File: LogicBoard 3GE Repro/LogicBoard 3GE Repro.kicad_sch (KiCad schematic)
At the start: 161 parts, among them IC201 27C512PLCC, IC204 CY62256-70PC, IC206 MC6809E, IC207 6522, IC208 YM2149, IC209 74HC74, IC301 MC1408, IC302 CD4052B, IC303 LF347, IC304 LF353, IC305 4066, J201 CART, J202 DB9_Male, J203 DB9_Male, J204 Power, J301 Video, J302 Audio, Q301 2N3905, Q302 2N3905, Q303 2N3904, SW201 Reset, U1 ATF16V8Bxx-xxPU

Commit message: Repro: on-board LM386 audio amp (anti-buzz) + external volume
Added IC306 LM386 audio amp on the logic board (next to YM2149, GNDA ref)
to avoid the cross-board low-level audio run that causes Vectrex buzz.
AUDIO -> J304 (panel volume pot) -> LM386 -> J303 speaker. Removed J302
line-out. ERC 11.

Co-Authored-By: Claude Opus 4.8 <noreply@anthropic.com>
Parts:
- removed C227: 22uF, Capacitor_SMD:C_1206_3216Metric, symbol Device:C_Polarized_Small
- removed C228: 22uF 16V, Capacitor_SMD:C_1206_3216Metric, symbol Device:C_Polarized_Small
- removed C323: 4.7uF 16V, Capacitor_SMD:C_0805_2012Metric, symbol Device:C_Polarized_Small
- removed J302: Audio, Connector_Molex:Molex_KK-254_AE-6410-02A_1x02_P2.54mm_Vertical, symbol Connector_Generic:Conn_01x02
- added C227, C228: 22uF, Capacitor_SMD:C_1206_3216Metric, symbol Device:C_Small
- added C323: 4.7uF 16V, Capacitor_SMD:C_0805_2012Metric, symbol Device:C_Small
- added C329, C331: 0.1uF, Capacitor_SMD:C_0402_1005Metric, symbol Device:C_Small
- added C330: 10uF, Capacitor_SMD:C_0402_1005Metric, symbol Device:C_Small
- added C332: C_Polarized_Small, symbol Device:C_Polarized_Small
- added C333: 47nF, Capacitor_SMD:C_0402_1005Metric, symbol Device:C_Small
- added IC306: LM386, symbol Amplifier_Audio:LM386
- added J303: Speaker, symbol Connector_Generic:Conn_01x02
- added J304: Volume, symbol Connector_Generic:Conn_01x03
- added R347: 10, symbol Device:R_Small
- added R348: 10K, symbol Device:R_Small
- D201, D301, D302: footprint (none) -> Diode_SMD:D_SOD-123
- IC201: footprint (none) -> Package_LCC:PLCC-32_THT-Socket
- IC202: renamed from U1; footprint (none) -> Package_SO:SOIC-20W_7.5x12.8mm_P1.27mm
- IC204: footprint (none) -> Package_SO:SOP-28_8.4x18.16mm_P1.27mm
- IC206, IC207: footprint (none) -> Package_LCC:PLCC-44_SMD-Socket
- IC208: footprint (none) -> Package_DIP:DIP-40_W15.24mm_Socket
- IC209, IC303, IC305: footprint (none) -> Package_SO:SOIC-14_3.9x8.7mm_P1.27mm
- IC301, IC302: footprint (none) -> Package_SO:SOIC-16_3.9x9.9mm_P1.27mm
- IC304: footprint (none) -> Package_SO:SOIC-8_3.9x4.9mm_P1.27mm
- J201: footprint (none) -> Vectrex LogicBoard:SULLINS_EBC18DRAS
- JP1, JP2, JP3: footprint (none) -> Connector_PinHeader_2.54mm:PinHeader_1x03_P2.54mm_Vertical
- Q301, Q302, Q303: footprint (none) -> Package_TO_SOT_SMD:SOT-23
- SW201: footprint (none) -> Connector_PinHeader_2.54mm:PinHeader_1x02_P2.54mm_Horizontal
- W1, W2, W3: footprint (none) -> NetTie:NetTie-2_SMD_Pad0.5mm
- Y201: renamed from OSC1; footprint (none) -> Oscillator:Oscillator_SMD_EuroQuartz_XO32-4Pin_3.2x2.5mm
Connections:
- net +5V: now also C227.1, C331.2, IC306.6 (V+)
- net AUDIO: now also J304.1 (Pin_1)
- net CH(A+B+C): now also C323.1
- net CH(A+B+C)+DIGITAL_AUDIO: now also C323.2
- net GNDA: now also C330.1, C331.1, C333.2, IC306.2 (-), IC306.4 (GND), J303.2 (Pin_2), J304.3 (Pin_3), R348.1
- net GNDD: now also C227.2, C228.2
- net ~{RESET}: now also C228.1
- new net: C330.2, IC306.7 (BYPASS)
- new net: C332.2, J303.1 (Pin_1)
- new net: C329.1, IC306.3 (+), R348.2
- new net: C329.2, J304.2 (Pin_2)
- new net: C332.1, IC306.5, R347.2
- new net: C333.1, R347.1
- no-connect marks 17 -> 18

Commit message: Repro: Phase 2 complete - all footprints assigned + audio amp
170 components, all footprints assigned (SMD 0402/SOIC/SOP/PLCC sockets,
3296W trimmers, LM386 audio amp). Integrator caps C0G, electrolytics
polarized, no polarity mismatches. Schematic + footprints done, ERC 11
(all intentional/trivial). Ready for PCB layout.

Co-Authored-By: Claude Opus 4.8 <noreply@anthropic.com>
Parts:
- C332, R348: footprint (none) -> Capacitor_SMD:CP_Elec_8x10.5
- IC306: footprint (none) -> Package_SO:SOIC-8_3.9x4.9mm_P1.27mm
- J303: footprint (none) -> Connector_PinHeader_2.54mm:PinHeader_1x02_P2.54mm_Vertical
- J304: footprint (none) -> Connector_PinHeader_2.54mm:PinHeader_1x03_P2.54mm_Vertical
- R302, R326, R333, R335: footprint Resistor_SMD:R_0402_1005Metric -> Potentiometer_THT:Potentiometer_Bourns_3296W_Vertical
- R347: footprint (none) -> Resistor_SMD:R_0402_1005Metric
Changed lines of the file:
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@@
 			)
 		)
-		(property "Footprint" "Resistor_SMD:R_0402_1005Metric"
+		(property "Footprint" "Potentiometer_THT:Potentiometer_Bourns_3296W_Vertical"
 			(at 146.05 147.32 0)
 			(hide yes)
@@
 			)
 		)
-		(property "Footprint" ""
+		(property "Footprint" "Connector_PinHeader_2.54mm:PinHeader_1x02_P2.54mm_Vertical"
 			(at 497.84 68.58 0)
 			(hide yes)
@@
 			)
 		)
-		(property "Footprint" ""
+		(property "Footprint" "Capacitor_SMD:CP_Elec_8x10.5"
 			(at 476.25 26.67 0)
 			(hide yes)
@@
 			)
 		)
-		(property "Footprint" ""
+		(property "Footprint" "Package_SO:SOIC-8_3.9x4.9mm_P1.27mm"
 			(at 491.49 39.37 0)
 			(hide yes)
@@
 			)
 		)
-		(property "Footprint" "Resistor_SMD:R_0402_1005Metric"
+		(property "Footprint" "Potentiometer_THT:Potentiometer_Bourns_3296W_Vertical"
 			(at 181.61 134.62 0)
 			(hide yes)
@@
 			)
 		)
-		(property "Footprint" "Resistor_SMD:R_0402_1005Metric"
+		(property "Footprint" "Potentiometer_THT:Potentiometer_Bourns_3296W_Vertical"
 			(at 181.61 255.27 0)
 			(hide yes)
@@
 			)
 		)
-		(property "Footprint" ""
+		(property "Footprint" "Resistor_SMD:R_0402_1005Metric"
 			(at 486.41 50.8 0)
 			(hide yes)
@@
 			)
 		)
-		(property "Footprint" ""
+		(property "Footprint" "Capacitor_SMD:CP_Elec_8x10.5"
 			(at 490.22 62.23 0)
 			(hide yes)
@@
 			)
 		)
-		(property "Footprint" ""
+		(property "Footprint" "Connector_PinHeader_2.54mm:PinHeader_1x03_P2.54mm_Vertical"
 			(at 491.49 7.62 0)
 			(hide yes)
@@
 			)
 		)
-		(property "Footprint" "Resistor_SMD:R_0402_1005Metric"
+		(property "Footprint" "Potentiometer_THT:Potentiometer_Bourns_3296W_Vertical"
 			(at 76.2 146.05 0)
 			(hide yes)

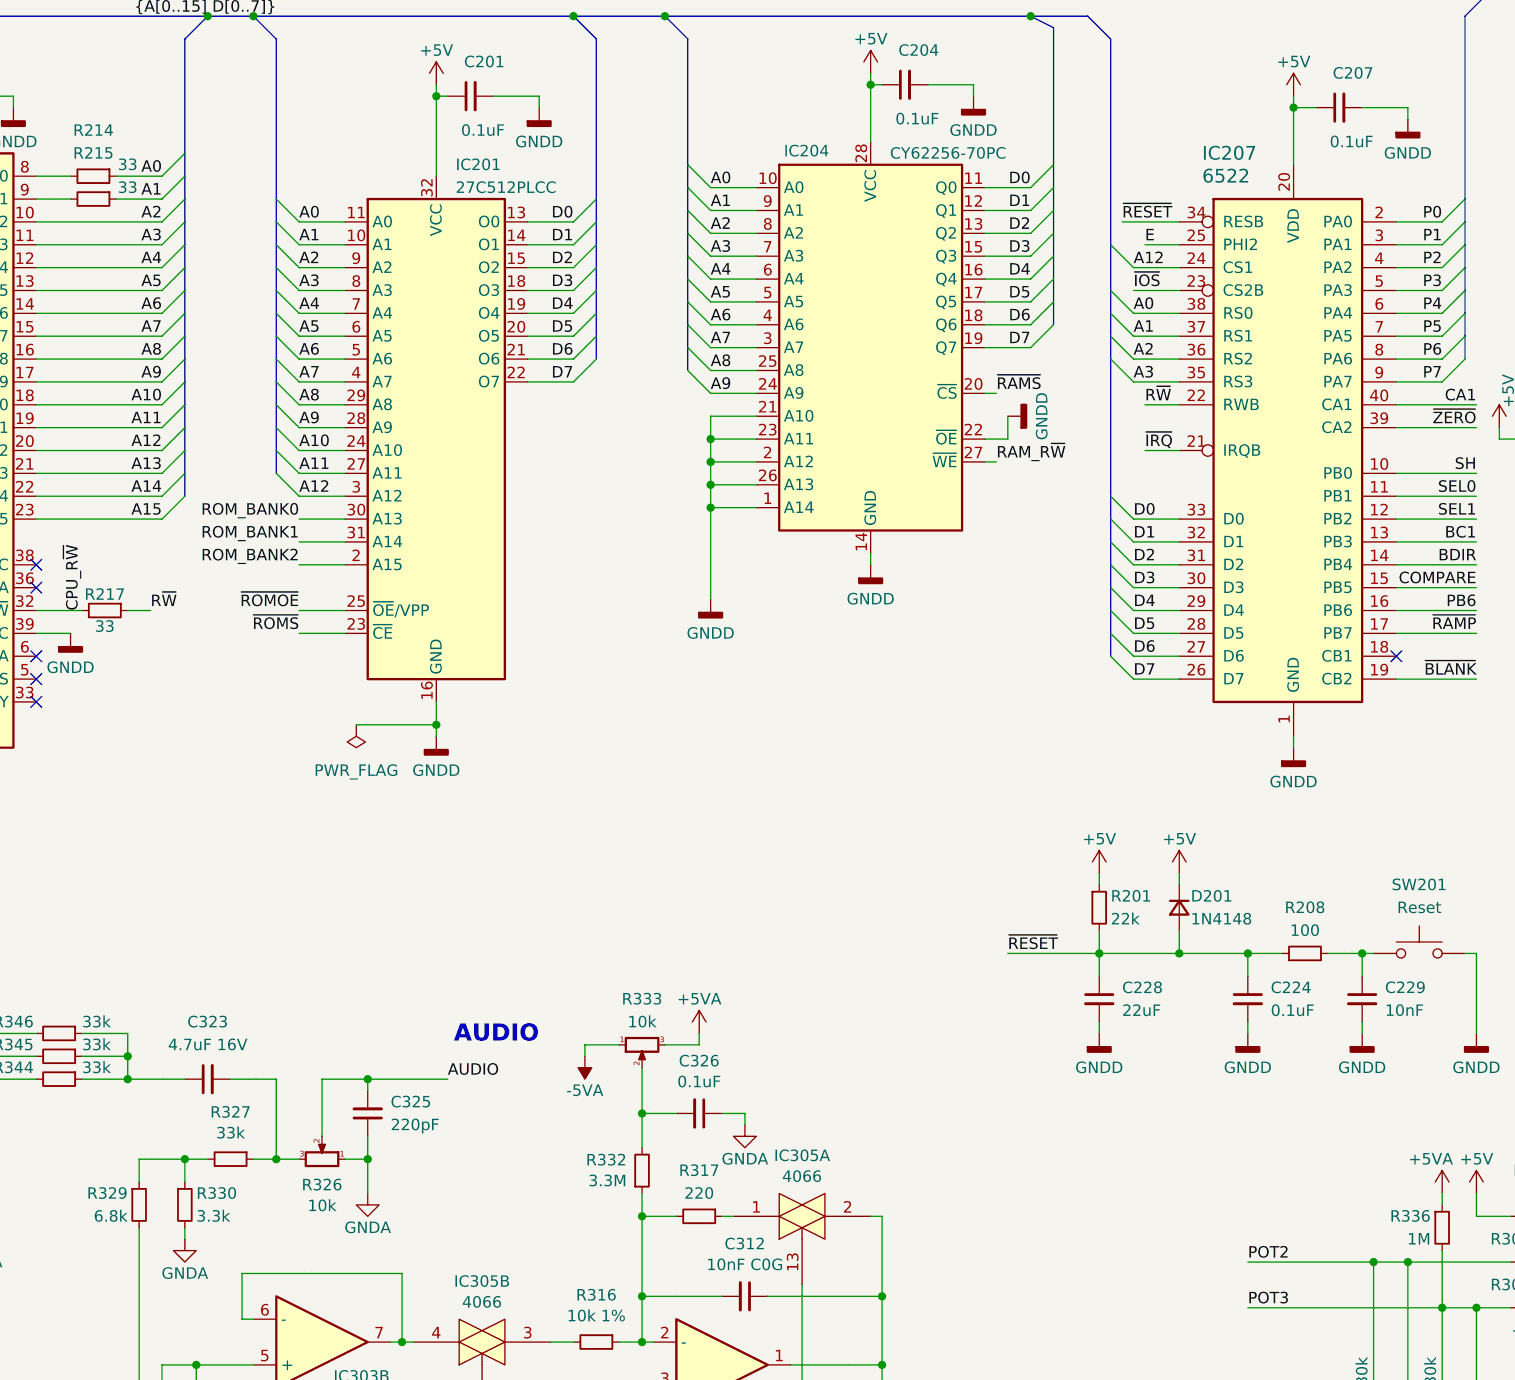
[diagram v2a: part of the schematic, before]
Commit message: Repro: remove redundant R326 volume pot (volume now single, in preamp)
R326 was the original Vectrex preamp volume pot; redundant now that the
external panel pot (J304) does it. Removed R326, merged the channel-mix
node into AUDIO -> J304 -> LM386. 3 calibration trimmers remain
(R302/R333/R335). ERC 11.

Co-Authored-By: Claude Opus 4.8 <noreply@anthropic.com>
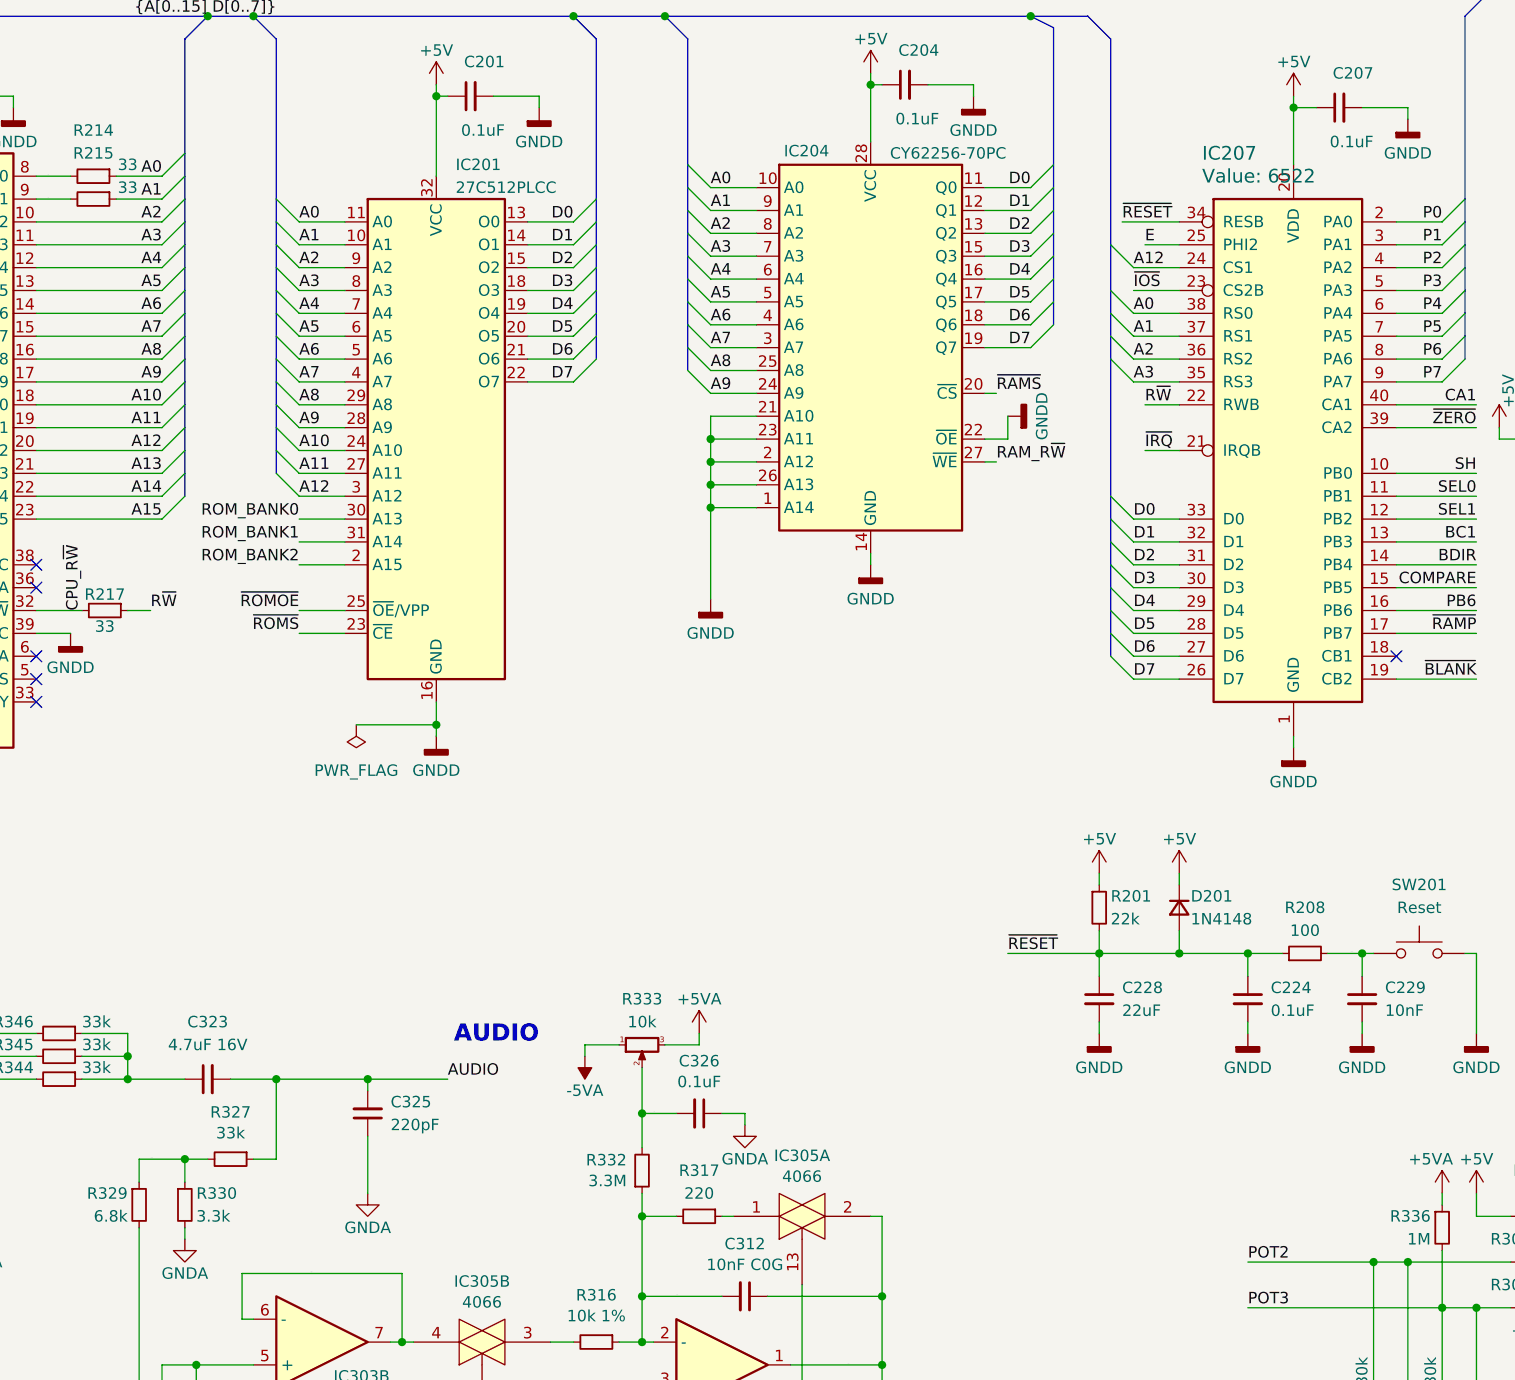
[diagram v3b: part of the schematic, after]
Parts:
- removed R326: 10k, Potentiometer_THT:Potentiometer_Bourns_3296W_Vertical, symbol Device:R_Potentiometer_Small
- R348: footprint Capacitor_SMD:CP_Elec_8x10.5 -> Resistor_SMD:R_0402_1005Metric
- SW201: footprint Connector_PinHeader_2.54mm:PinHeader_1x02_P2.54mm_Horizontal -> Connector_PinHeader_2.54mm:PinHeader_1x02_P2.54mm_Vertical
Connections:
- net CH(A+B+C)+DIGITAL_AUDIO is gone; now on net AUDIO: C323.2, R327.1
- net CH(A+B+C): no longer names the net of C323.1, R344.1, R345.1, R346.1
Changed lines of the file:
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@@
 	)
 	(junction
-		(at 151.13 147.32)
-		(diameter 0)
-		(color 0 0 0 0)
-	)
-	(junction
 		(at 36.83 196.85)
 		(diameter 0)
@@
 	)
 	(junction
-		(at 140.97 147.32)
-		(diameter 0)
-		(color 0 0 0 0)
-	)
-	(junction
 		(at 323.85 148.59)
 		(diameter 0)
@@
 	)
 	(junction
+		(at 140.97 138.43)
+		(diameter 0)
+		(color 0 0 0 0)
+	)
+	(junction
 		(at 328.93 223.52)
 		(diameter 0)
@@
 	(wire
 		(pts
+			(xy 140.97 138.43) (xy 140.97 147.32)
+		)
+		(stroke
+			(width 0)
+			(type default)
+		)
+	)
+	(wire
+		(pts
 			(xy 355.6 153.67) (xy 355.6 184.15)
 		)
@@
 	(wire
 		(pts
-			(xy 140.97 147.32) (xy 143.51 147.32)
-		)
-		(stroke
-			(width 0)
-			(type default)
-		)
-	)
-	(wire
-		(pts
 			(xy 45.72 55.88) (xy 55.88 55.88)
 		)
@@
 	(wire
 		(pts
-			(xy 151.13 147.32) (xy 151.13 151.13)
+			(xy 151.13 144.78) (xy 151.13 151.13)
 		)
 		(stroke
@@
 	(wire
 		(pts
-			(xy 151.13 144.78) (xy 151.13 147.32)
-		)
-		(stroke
-			(width 0)
-			(type default)
-		)
-	)
-	(wire
-		(pts
 			(xy 347.98 172.72) (xy 367.03 172.72)
 		)
@@
 	(wire
 		(pts
-			(xy 140.97 147.32) (xy 140.97 138.43)
-		)
-		(stroke
-			(width 0)
-			(type default)
-		)
-	)
-	(wire
-		(pts
 			(xy 270.51 151.13) (xy 270.51 152.4)
 		)
@@
 	(wire
 		(pts
-			(xy 148.59 147.32) (xy 151.13 147.32)
-		)
-		(stroke
-			(width 0)
-			(type default)
-		)
-	)
-	(wire
-		(pts
 			(xy 189.23 46.99) (xy 194.31 46.99)
 		)
@@
 	(wire
 		(pts
-			(xy 146.05 138.43) (xy 151.13 138.43)
-		)
-		(stroke
-			(width 0)
-			(type default)
-		)
-	)
-	(wire
-		(pts
 			(xy 114.3 63.5) (xy 128.27 63.5)
 		)
@@
 	(wire
 		(pts
+			(xy 135.89 138.43) (xy 151.13 138.43)
+		)
+		(stroke
+			(width 0)
+			(type default)
+		)
+	)
+	(wire
+		(pts
 			(xy 45.72 66.04) (xy 55.88 66.04)
 		)
@@
 	(wire
 		(pts
-			(xy 146.05 138.43) (xy 146.05 144.78)
-		)
-		(stroke
-			(width 0)
-			(type default)
-		)
-	)
-	(wire
-		(pts
 			(xy 317.5 218.44) (xy 317.5 223.52)
 		)
@@
 	(wire
 		(pts
-			(xy 140.97 138.43) (xy 135.89 138.43)
-		)
-		(stroke
-			(width 0)
-			(type default)
-		)
-	)
-	(wire
-		(pts
 			(xy 143.51 88.9) (xy 148.59 88.9)
 		)
@@
 		)
 	)
-	(label "CH(A+B+C)+DIGITAL_AUDIO"
-		(at 138.43 138.43 0)
-		(effects
-			(font
-				(size 0.0254 0.0254)
-			)
-			(justify left bottom)
-		)
-	)
 	(label "RAM_R~{W}"
 		(at 220.98 69.85 0)
@@
 		)
 	)
-	(label "CH(A+B+C)"
-		(at 128.27 138.43 0)
-		(effects
-			(font
-				(size 0.0254 0.0254)
-			)
-			(justify left bottom)
-		)
-	)
 	(label "A2"
 		(at 189.23 44.45 0)
@@
 	)
 	(symbol
-		(lib_id "Device:R_Potentiometer_Small")
-		(at 146.05 147.32 270)
-		(mirror x)
-		(unit 1)
-		(body_style 1)
-		(exclude_from_sim no)
-		(in_bom yes)
-		(on_board yes)
-		(in_pos_files yes)
-		(dnp no)
-		(property "Reference" "R326"
-			(at 146.05 150.1902 90)
-			(show_name no)
-			(do_not_autoplace no)
-			(effects
-				(font
-					(size 1.27 1.27)
-				)
-			)
-		)
-		(property "Value" "10k"
-			(at 146.05 152.5016 90)
-			(show_name no)
-			(do_not_autoplace no)
-			(effects
-				(font
-					(size 1.27 1.27)
-				)
-			)
-		)
-		(property "Footprint" "Potentiometer_THT:Potentiometer_Bourns_3296W_Vertical"
-			(at 146.05 147.32 0)
-			(hide yes)
-			(show_name no)
-			(do_not_autoplace no)
-			(effects
-				(font
-					(size 1.27 1.27)
-				)
-			)
-		)
-		(property "Datasheet" ""
-			(at 146.05 147.32 0)
-			(hide yes)
-			(show_name no)
-			(do_not_autoplace no)
-			(effects
-				(font
-					(size 1.27 1.27)
-				)
-			)
-		)
-		(property "Description" "Potentiometer"
-			(at 146.05 147.32 0)
-			(hide yes)
-			(show_name no)
-			(do_not_autoplace no)
-			(effects
-				(font
-					(size 1.27 1.27)
-				)
-			)
-		)
-		(property "Mouser" "531-PT10H-10k-S"
-			(at 113.03 303.53 0)
-			(hide yes)
-			(show_name no)
-			(do_not_autoplace no)
-			(effects
-				(font
-					(size 1.27 1.27)
-				)
-			)
-		)
-		(property "Sim.Device" "R"
-			(at 146.05 147.32 0)
-			(hide yes)
-			(show_name no)
-			(do_not_autoplace no)
-			(effects
-				(font
-					(size 1.27 1.27)
-				)
-			)
-		)
-		(property "Sim.Type" "POT"
-			(at 146.05 147.32 0)
-			(hide yes)
-			(show_name no)
-			(do_not_autoplace no)
-			(effects
-				(font
-					(size 1.27 1.27)
-				)
-			)
-		)
-		(property "Sim.Pins" "1=r0 2=wiper 3=r1"
-			(at 146.05 147.32 0)
-			(hide yes)
-			(show_name no)
-			(do_not_autoplace no)
-			(effects
-				(font
-					(size 1.27 1.27)
-				)
-			)
-		)
-		(pin "1"
-		)
-		(pin "2"
-		)
-		(pin "3"
-		)
-		(instances
-			(project "LogicBoard 3GE Repro"
-				(path "/e63e39d7-6ac0-4ffd-8aa3-1841a4541b55"
-					(reference "R326")
-					(unit 1)
-				)
-			)
-		)
-	)
-	(symbol
 		(lib_id "Device:C_Small")
 		(at 314.96 181.61 90)
@@
 			)
 		)
-		(property "Footprint" "Capacitor_SMD:CP_Elec_8x10.5"
+		(property "Footprint" "Resistor_SMD:R_0402_1005Metric"
 			(at 476.25 26.67 0)
 			(hide yes)
@@
 			)
 		)
-		(property "Footprint" "Connector_PinHeader_2.54mm:PinHeader_1x02_P2.54mm_Horizontal"
+		(property "Footprint" "Connector_PinHeader_2.54mm:PinHeader_1x02_P2.54mm_Vertical"
 			(at 267.97 119.38 0)
 			(hide yes)
@@
 		(property "Value" "6522"
 			(at 243.84 38.1 0)
-			(show_name no)
+			(show_name yes)
 			(do_not_autoplace no)
 			(effects
